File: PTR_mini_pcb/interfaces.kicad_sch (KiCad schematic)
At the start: 21 parts, among them J14 Molex 104031-0811, J4 USB4105-GF-A-120, U11 USBLC6-2SC6-ES, U13 W25Q256

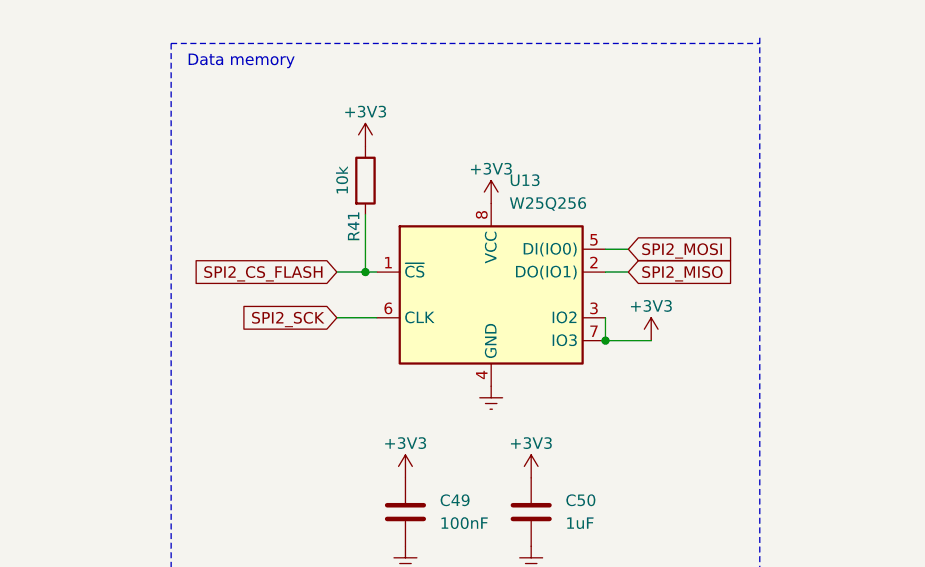
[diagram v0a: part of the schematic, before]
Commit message: SPI Flash moved to different SPI lines
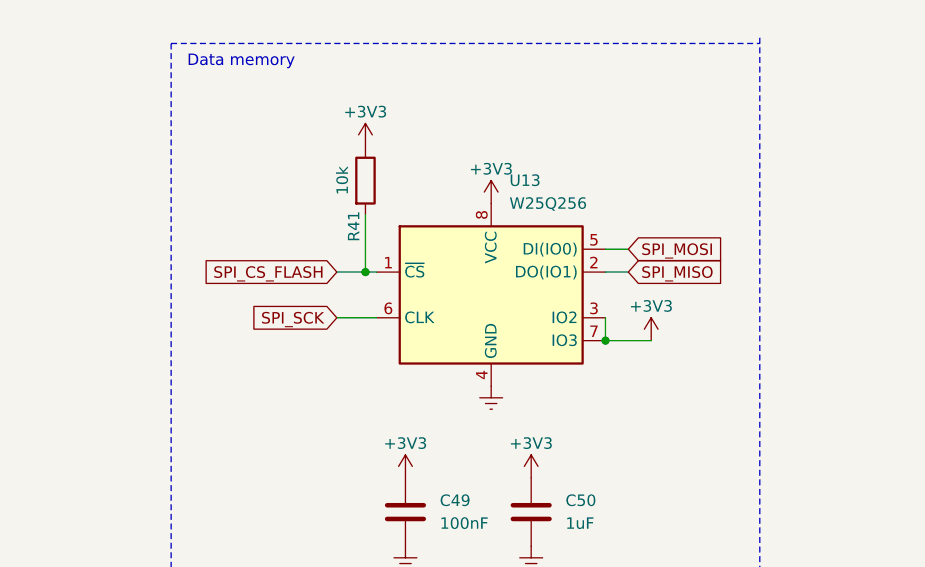
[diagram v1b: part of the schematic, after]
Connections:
- net SPI2_MISO: no longer U13.2 (DO(IO1))
- net SPI2_MOSI: no longer U13.5 (DI(IO0))
- net SPI2_SCK: no longer U13.6 (CLK)
- net SPI2_CS_FLASH renamed SPI_CS_FLASH
- new net SPI_MISO: U13.2 (DO(IO1))
- new net SPI_MOSI: U13.5 (DI(IO0))
- new net SPI_SCK: U13.6 (CLK)
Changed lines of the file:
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@@
+		)
+	)
+	(global_label "SPI_MOSI"
+		(shape input)
+		(at 95.25 123.19 0)
+		(fields_autoplaced yes)
+		(effects
+			(font
+				(size 1.27 1.27)
+			)
+			(justify left)
+		)
+		(property "Intersheetrefs" "${INTERSHEET_REFS}"
+			(at 106.8833 123.19 0)
+			(hide yes)
+			(show_name no)
+			(do_not_autoplace no)
+			(effects
+				(font
+					(size 1.27 1.27)
+				)
+				(justify left)
+			)
+		)
+	)
+	(global_label "SPI2_CS_SD"
+		(shape input)
+		(at 148.59 125.73 180)
+		(fields_autoplaced yes)
+		(effects
+			(font
+				(size 1.27 1.27)
+			)
+			(justify right)
+		)
+		(property "Intersheetrefs" "${INTERSHEET_REFS}"
+			(at 134.4168 125.73 0)
+			(hide yes)
+			(show_name no)
+			(do_not_autoplace no)
+			(effects
+				(font
+					(size 1.27 1.27)
+				)
+				(justify right)
+			)
+		)
+	)
+	(global_label "SPI_CS_FLASH"
+		(shape input)
+		(at 62.865 125.73 180)
+		(fields_autoplaced yes)
+		(effects
+			(font
+				(size 1.27 1.27)
+			)
+			(justify right)
+		)
+		(property "Intersheetrefs" "${INTERSHEET_REFS}"
+			(at 46.6355 125.73 0)
+			(hide yes)
+			(show_name no)
+			(do_not_autoplace no)
+			(effects
+				(font
+					(size 1.27 1.27)
+				)
+				(justify right)
+			)
+		)
+	)
+	(global_label "USB_DM"
+		(shape input)
+		(at 30.48 42.545 180)
+		(fields_autoplaced yes)
+		(effects
+			(font
+				(size 1.27 1.27)
+			)
+			(justify right)
+		)
+		(property "Intersheetrefs" "${INTERSHEET_REFS}"
+			(at 20.5679 42.4656 0)
+			(hide yes)
+			(show_name no)
+			(do_not_autoplace no)
+			(effects
+				(font
+					(size 1.27 1.27)
+				)
+				(justify right)
+			)
+		)
+	)
+	(global_label "USB_DP"
+		(shape input)
+		(at 30.48 45.085 180)
+		(fields_autoplaced yes)
+		(effects
+			(font
+				(size 1.27 1.27)
+			)
+			(justify right)
+		)
+		(property "Intersheetrefs" "${INTERSHEET_REFS}"
+			(at 20.7493 45.0056 0)
+			(hide yes)
+			(show_name no)
+			(do_not_autoplace no)
+			(effects
+				(font
+					(size 1.27 1.27)
+				)
+				(justify right)
+			)
+		)
+	)
+	(global_label "SPI_SCK"
+		(shape input)
+		(at 62.865 130.81 180)
+		(fields_autoplaced yes)
+		(effects
+			(font
+				(size 1.27 1.27)
+			)
+			(justify right)
+		)
+		(property "Intersheetrefs" "${INTERSHEET_REFS}"
+			(at 52.0784 130.81 0)
+			(hide yes)
+			(show_name no)
+			(do_not_autoplace no)
+			(effects
+				(font
+					(size 1.27 1.27)
+				)
+				(justify right)
+			)
 		)
 	)
 	(global_label "SPI2_MOSI"
 		(shape input)
-		(at 95.25 123.19 0)
+		(at 148.59 128.27 180)
+		(fields_autoplaced yes)
+		(effects
+			(font
+				(size 1.27 1.27)
+			)
+			(justify right)
+		)
+		(property "Intersheetrefs" "${INTERSHEET_REFS}"
+			(at 135.7472 128.27 0)
+			(hide yes)
+			(show_name no)
+			(do_not_autoplace no)
+			(effects
+				(font
+					(size 1.27 1.27)
+				)
+				(justify right)
+			)
+		)
+	)
+	(global_label "SPI2_DET"
+		(shape input)
+		(at 148.59 143.51 180)
+		(fields_autoplaced yes)
+		(effects
+			(font
+				(size 1.27 1.27)
+			)
+			(justify right)
+		)
+		(property "Intersheetrefs" "${INTERSHEET_REFS}"
+			(at 136.9568 143.51 0)
+			(hide yes)
+			(show_name no)
+			(do_not_autoplace no)
+			(effects
+				(font
+					(size 1.27 1.27)
+				)
+				(justify right)
+			)
+		)
+	)
+	(global_label "SPI2_MISO"
+		(shape input)
+		(at 148.59 138.43 180)
+		(fields_autoplaced yes)
+		(effects
+			(font
+				(size 1.27 1.27)
+			)
+			(justify right)
+		)
+		(property "Intersheetrefs" "${INTERSHEET_REFS}"
+			(at 135.7472 138.43 0)
+			(hide yes)
+			(show_name no)
+			(do_not_autoplace no)
+			(effects
+				(font
+					(size 1.27 1.27)
+				)
+				(justify right)
+			)
+		)
+	)
+	(global_label "SPI_MISO"
+		(shape input)
+		(at 95.25 125.73 0)
 		(fields_autoplaced yes)
 		(effects
@@
 		)
 		(property "Intersheetrefs" "${INTERSHEET_REFS}"
-			(at 108.0928 123.19 0)
-			(hide yes)
-			(show_name no)
-			(do_not_autoplace no)
-			(effects
-				(font
-					(size 1.27 1.27)
-				)
-				(justify left)
-			)
-		)
-	)
-	(global_label "SPI2_CS_SD"
-		(shape input)
-		(at 148.59 125.73 180)
-		(fields_autoplaced yes)
-		(effects
-			(font
-				(size 1.27 1.27)
-			)
-			(justify right)
-		)
-		(property "Intersheetrefs" "${INTERSHEET_REFS}"
-			(at 134.4168 125.73 0)
-			(hide yes)
-			(show_name no)
-			(do_not_autoplace no)
-			(effects
-				(font
-					(size 1.27 1.27)
-				)
-				(justify right)
-			)
-		)
-	)
-	(global_label "SPI2_CS_FLASH"
-		(shape input)
-		(at 62.865 125.73 180)
-		(fields_autoplaced yes)
-		(effects
-			(font
-				(size 1.27 1.27)
-			)
-			(justify right)
-		)
-		(property "Intersheetrefs" "${INTERSHEET_REFS}"
-			(at 45.426 125.73 0)
-			(hide yes)
-			(show_name no)
-			(do_not_autoplace no)
-			(effects
-				(font
-					(size 1.27 1.27)
-				)
-				(justify right)
-			)
-		)
-	)
-	(global_label "USB_DM"
-		(shape input)
-		(at 30.48 42.545 180)
-		(fields_autoplaced yes)
-		(effects
-			(font
-				(size 1.27 1.27)
-			)
-			(justify right)
-		)
-		(property "Intersheetrefs" "${INTERSHEET_REFS}"
-			(at 20.5679 42.4656 0)
-			(hide yes)
-			(show_name no)
-			(do_not_autoplace no)
-			(effects
-				(font
-					(size 1.27 1.27)
-				)
-				(justify right)
-			)
-		)
-	)
-	(global_label "USB_DP"
-		(shape input)
-		(at 30.48 45.085 180)
-		(fields_autoplaced yes)
-		(effects
-			(font
-				(size 1.27 1.27)
-			)
-			(justify right)
-		)
-		(property "Intersheetrefs" "${INTERSHEET_REFS}"
-			(at 20.7493 45.0056 0)
-			(hide yes)
-			(show_name no)
-			(do_not_autoplace no)
-			(effects
-				(font
-					(size 1.27 1.27)
-				)
-				(justify right)
-			)
-		)
-	)
-	(global_label "SPI2_SCK"
-		(shape input)
-		(at 62.865 130.81 180)
-		(fields_autoplaced yes)
-		(effects
-			(font
-				(size 1.27 1.27)
-			)
-			(justify right)
-		)
-		(property "Intersheetrefs" "${INTERSHEET_REFS}"
-			(at 50.8689 130.81 0)
-			(hide yes)
-			(show_name no)
-			(do_not_autoplace no)
-			(effects
-				(font
-					(size 1.27 1.27)
-				)
-				(justify right)
-			)
-		)
-	)
-	(global_label "SPI2_MOSI"
-		(shape input)
-		(at 148.59 128.27 180)
-		(fields_autoplaced yes)
-		(effects
-			(font
-				(size 1.27 1.27)
-			)
-			(justify right)
-		)
-		(property "Intersheetrefs" "${INTERSHEET_REFS}"
-			(at 135.7472 128.27 0)
-			(hide yes)
-			(show_name no)
-			(do_not_autoplace no)
-			(effects
-				(font
-					(size 1.27 1.27)
-				)
-				(justify right)
-			)
-		)
-	)
-	(global_label "SPI2_DET"
-		(shape input)
-		(at 148.59 143.51 180)
-		(fields_autoplaced yes)
-		(effects
-			(font
-				(size 1.27 1.27)
-			)
-			(justify right)
-		)
-		(property "Intersheetrefs" "${INTERSHEET_REFS}"
-			(at 136.9568 143.51 0)
-			(hide yes)
-			(show_name no)
-			(do_not_autoplace no)
-			(effects
-				(font
-					(size 1.27 1.27)
-				)
-				(justify right)
-			)
-		)
-	)
-	(global_label "SPI2_MISO"
-		(shape input)
-		(at 148.59 138.43 180)
-		(fields_autoplaced yes)
-		(effects
-			(font
-				(size 1.27 1.27)
-			)
-			(justify right)
-		)
-		(property "Intersheetrefs" "${INTERSHEET_REFS}"
-			(at 135.7472 138.43 0)
-			(hide yes)
-			(show_name no)
-			(do_not_autoplace no)
-			(effects
-				(font
-					(size 1.27 1.27)
-				)
-				(justify right)
-			)
-		)
-	)
-	(global_label "SPI2_MISO"
-		(shape input)
-		(at 95.25 125.73 0)
-		(fields_autoplaced yes)
-		(effects
-			(font
-				(size 1.27 1.27)
-			)
-			(justify left)
-		)
-		(property "Intersheetrefs" "${INTERSHEET_REFS}"
-			(at 108.0928 125.73 0)
-			(hide yes)
-			(show_name no)
+			(at 106.8833 125.73 0)
+			(hide yes)
+			(show_name no)

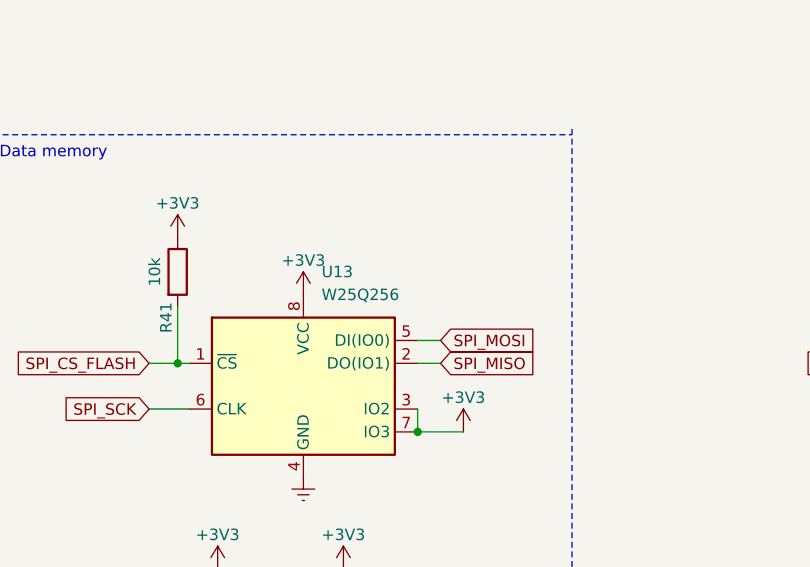
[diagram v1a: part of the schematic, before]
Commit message: +Flash model changed
+new step models
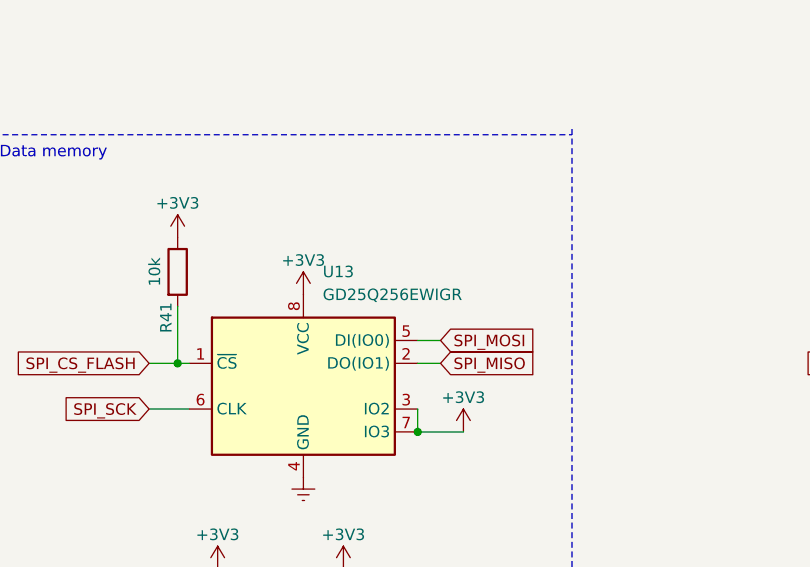
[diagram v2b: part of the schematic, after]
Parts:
- U13: value W25Q256 -> GD25Q256EWIGR
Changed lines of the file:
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@@
 		(fields_autoplaced yes)
 		(property "Reference" "U13"
-			(at 82.0294 115.57 0)
+			(at 82.1533 115.57 0)
 			(show_name no)
 			(do_not_autoplace no)
@@
 			)
 		)
-		(property "Value" "W25Q256"
-			(at 82.0294 118.11 0)
+		(property "Value" "GD25Q256EWIGR"
+			(at 82.1533 118.11 0)
 			(show_name no)
 			(do_not_autoplace no)
